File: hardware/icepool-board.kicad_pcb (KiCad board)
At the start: 4 copper layers, 66 x 58 mm, 185 parts, among them J1 USB Micro, J2 PWR_IN, J3 SWD, J4 I2C, J5 RS485, SW1 B3U-1000P, U1 ATSAMD21E, U2 ISL83485, U3 iCE40HX8K-BG121(121-Ball_caBG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, U4 iCE40HX8K-BG121(121-Ball_caBG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, U5 iCE40HX8K-BG121(121-Ball_caBG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, U6 iCE40HX8K-BG121(121-Ball_caBG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, U7 FAN2306, U8 TPS715_SC70, U9 FAN2306, X1 CB3LV-3I-16M0000, X2 CB3LV-3I-16M0000, X3 CB3LV-3I-16M0000, X4 CB3LV-3I-16M0000, Y1 16MHz

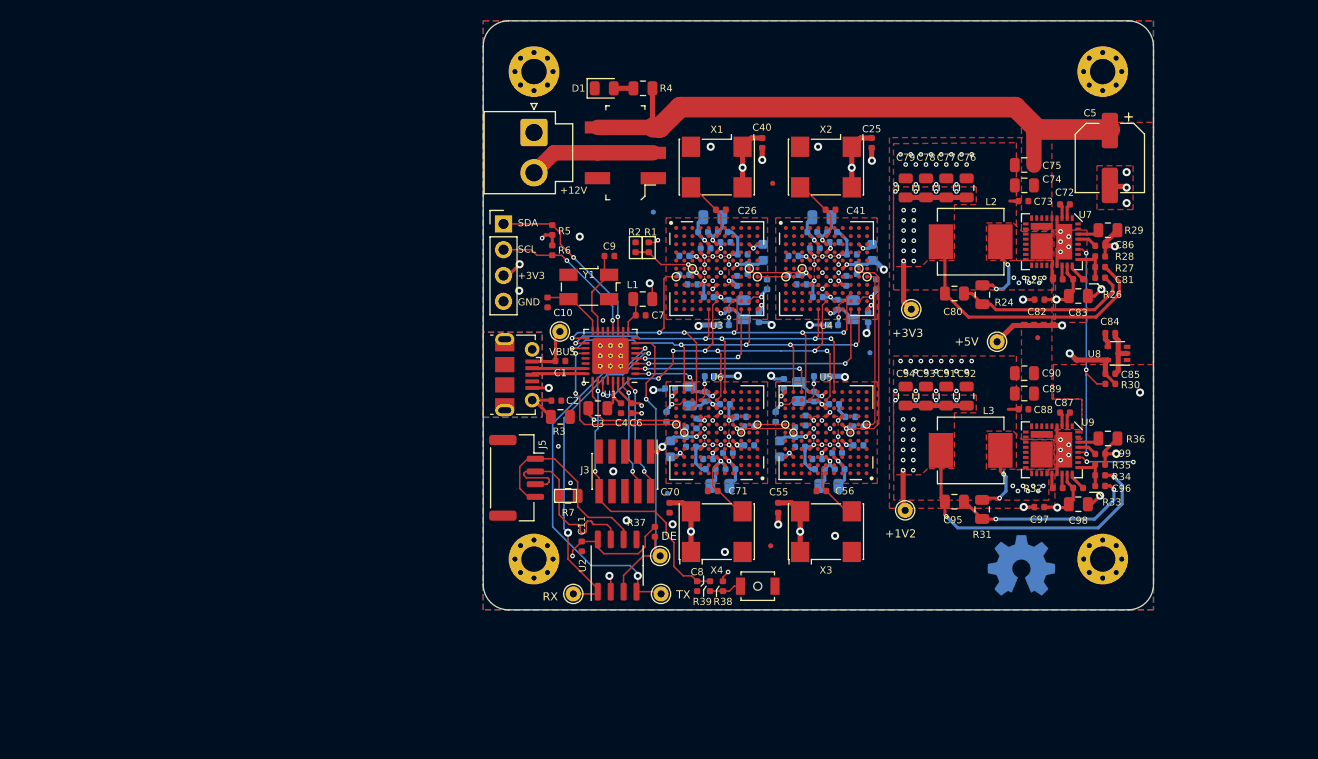
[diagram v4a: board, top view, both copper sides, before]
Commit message: Starting to re-layout. Removed PWR switch.
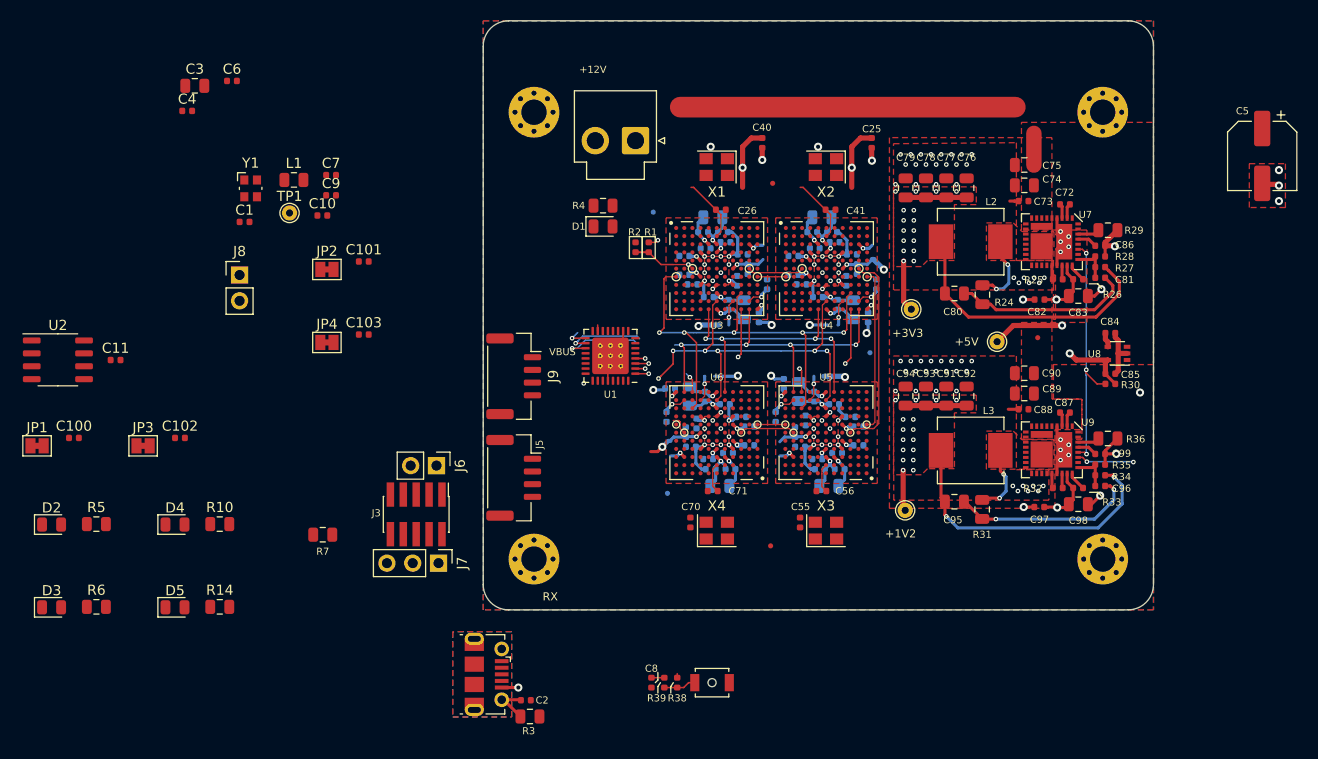
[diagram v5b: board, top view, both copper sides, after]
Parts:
- removed J4: I2C, Connector_PinHeader_2.54mm:PinHeader_1x04_P2.54mm_Vertical
- removed R18, R22, R37: 4k7, Resistor_SMD:R_0402_1005Metric
- removed REF**: OSHW-Symbol_6.7x6mm_Copper, Symbol:OSHW-Symbol_6.7x6mm_Copper
- removed S1: JS202011SCQN, digikey-footprints:Switch_Slide_JS202011SCQN
- removed TP2: RX, TestPoint:TestPoint_THTPad_D1.5mm_Drill0.7mm
- removed TP3: TX, TestPoint:TestPoint_THTPad_D1.5mm_Drill0.7mm
- removed TP7: DE, TestPoint:TestPoint_THTPad_D1.5mm_Drill0.7mm
- added C100: 0.1u, Capacitor_SMD:C_0402_1005Metric, F.Cu at (69.7, 123.1)
- added C101: 0.1u, Capacitor_SMD:C_0402_1005Metric, F.Cu at (98.2, 105.7)
- added C102: 0.1u, Capacitor_SMD:C_0402_1005Metric, F.Cu at (80.1, 123.1)
- added C103: 0.1u, Capacitor_SMD:C_0402_1005Metric, F.Cu at (98.2, 112.9)
- added J6: PWR_ALT, Connector_PinHeader_2.54mm:PinHeader_1x02_P2.54mm_Vertical, F.Cu at (105.4, 125.8)
- added J7: SWD_ALT, Connector_PinHeader_2.54mm:PinHeader_1x03_P2.54mm_Vertical, F.Cu at (105.6, 135.4)
- added J8: UART, Connector_PinHeader_2.54mm:PinHeader_1x02_P2.54mm_Vertical, F.Cu at (86.0, 107.0)
- added J9: RS485_OUT, Connector_JST:JST_GH_SM04B-GHS-TB_1x04-1MP_P1.25mm_Horizontal, F.Cu at (113.0, 117.0)
- added JP1: CUT_2V5, Jumper:SolderJumper-2_P1.3mm_Bridged_Pad1.0x1.5mm, F.Cu at (66.1, 123.8)
- added JP2: CUT_2V5, Jumper:SolderJumper-2_P1.3mm_Bridged_Pad1.0x1.5mm, F.Cu at (94.6, 106.5)
- added JP3: CUT_2V5, Jumper:SolderJumper-2_P1.3mm_Bridged_Pad1.0x1.5mm, F.Cu at (76.5, 123.8)
- added JP4: CUT_2V5, Jumper:SolderJumper-2_P1.3mm_Bridged_Pad1.0x1.5mm, F.Cu at (94.6, 113.7)
- C10, C9: value 15p -> 8p
- C26, C41, C56, C71: value 22p -> DNP
- D2, D3, D4, D5: value CDBU0520 -> LED_IND; footprint Diode_SMD:D_0603_1608Metric -> LED_SMD:LED_0805_2012Metric; moved to F.Cu
- J5: value RS485 -> RS485_IN
- R10, R14: value 4k7 -> 1k; footprint Resistor_SMD:R_0402_1005Metric -> Resistor_SMD:R_0805_2012Metric; moved to F.Cu
- R25, R32: value 1.54k -> 1.50k
- R29: value 56R -> 56k
- R36: value 20R -> 20k
- R5, R6: value 4k7 -> 1k; footprint Resistor_SMD:R_0402_1005Metric -> Resistor_SMD:R_0805_2012Metric
- U2: value ISL83485 -> ISL83488
- X1, X2, X3, X4: value CB3LV-3I-16M0000 -> ASEM1-12.000MHZ; footprint Oscillator:Oscillator_SMD_Abracon_ASV-4Pin_7.0x5.1mm -> Oscillator:Oscillator_SMD_Abracon_ASE-4Pin_3.2x2.5mm
- Y1: footprint Crystal:Crystal_SMD_Abracon_ABM3B-4Pin_5.0x3.2mm -> Crystal:Crystal_SMD_Abracon_ABM10-4Pin_2.5x2.0mm
- moved D3 88.0 mm to (67.5, 139.8), turned to 0 degrees
- moved D2 75.0 mm to (67.5, 131.6), turned to 0 degrees
- moved R14 66.5 mm to (84.1, 139.7)
- moved D4 60.0 mm to (79.7, 131.6), turned to 0 degrees
- moved U2 58.7 mm to (68.1, 115.4), turned to 0 degrees
- moved R6 57.0 mm to (71.9, 139.7), turned to 0 degrees
- moved R5 53.4 mm to (71.9, 131.6), turned to 0 degrees
- moved R10 53.4 mm to (84.1, 131.6)
- moved C4 51.8 mm to (80.8, 90.9), turned to 0 degrees
- moved D5 51.2 mm to (79.7, 139.8), turned to 0 degrees
- moved C6 50.8 mm to (85.3, 87.9), turned to 0 degrees
- moved C3 50.8 mm to (81.6, 88.4)
- moved C11 49.4 mm to (73.8, 115.4), turned to 0 degrees
- moved L1 36.3 mm to (91.4, 97.7)
- moved Y1 34.7 mm to (87.1, 98.5), turned to 0 degrees
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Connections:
- D2 pad 1: /ICE40HX8K-BG121_0/VPP_2V5 -> /ICE40HX8K-BG121_0/LED_IND
- D2 pad 2: +3V3 -> Net-(D2-Pad2)
- D3 pad 1: /ICE40HX8K-BG121_1/VPP_2V5 -> /ICE40HX8K-BG121_1/LED_IND
- D3 pad 2: +3V3 -> Net-(D3-Pad2)
- D4 pad 1: /ICE40HX8K-BG121_2/VPP_2V5 -> /ICE40HX8K-BG121_2/LED_IND
- D4 pad 2: +3V3 -> Net-(D4-Pad2)
- D5 pad 1: /ICE40HX8K-BG121_3/VPP_2V5 -> /ICE40HX8K-BG121_3/LED_IND
- D5 pad 2: +3V3 -> Net-(D5-Pad2)
- J5 pad 1: /DS+ -> /RX+
- J5 pad 2: /DS- -> /RX-
- J5 pad 3: /DS- -> /TX+
- J5 pad 4: /DS+ -> /TX-
- R10 pad 1: +3V3 -> Net-(D4-Pad2)
- R10 pad 2: Net-(R10-Pad2) -> +3V3
- R11 pad 2: /ICE40HX8K-BG121_0/SPI_SS_B -> /SPI_SS_B_0
- R14 pad 1: +3V3 -> Net-(D5-Pad2)
- R14 pad 2: Net-(R14-Pad2) -> +3V3
- R15 pad 2: /ICE40HX8K-BG121_1/SPI_SS_B -> /SPI_SS_B_1
- R19 pad 2: /ICE40HX8K-BG121_2/SPI_SS_B -> /SPI_SS_B_2
- R23 pad 2: /ICE40HX8K-BG121_3/SPI_SS_B -> /SPI_SS_B_3
- R5 pad 1: +3V3 -> Net-(D2-Pad2)
- R5 pad 2: /I2C_SDA -> +3V3
- R6 pad 1: +3V3 -> Net-(D3-Pad2)
- R6 pad 2: /I2C_SCL -> +3V3
- R7 pad 1: /DS+ -> /RX-
- R7 pad 2: /DS- -> /RX+
- U1 pad 1: /CRESET_B_3 -> /SPI_SS_B_3
- U1 pad 13: Net-(U1-Pad13) -> /CDONE
- U1 pad 14: Net-(U1-Pad14) -> /CRESET_B
- U1 pad 2: /CRESET_B_2 -> /SPI_SS_B_2
- U1 pad 3: /CRESET_B_1 -> /SPI_SS_B_1
- U1 pad 4: /CRESET_B_0 -> /SPI_SS_B_0
- U1 pad 5: /RX -> /TX
- U1 pad 6: /TX -> /XCK
- U1 pad 7: /DE -> /RX
- U2 pad 1: /RX -> +3V3
- U2 pad 2: GND -> /RX
- U2 pad 3: /DE -> /TX
- U2 pad 4: /TX -> GND
- U2 pad 5: GND -> /TX-
- U2 pad 6: /DS+ -> /TX+
- U2 pad 7: /DS- -> /RX-
- U2 pad 8: +3V3 -> /RX+
- U3 pad A11: Net-(U3-PadA11) -> /ICE40HX8K-BG121_0/LED_IND
- U3 pad K10: /ICE40HX8K-BG121_0/SPI_SS_B -> /SPI_SS_B_0
- U3 pad K8: Net-(R10-Pad2) -> /CDONE
- U3 pad L9: /CRESET_B_0 -> /CRESET_B
- U4 pad A11: Net-(U4-PadA11) -> /ICE40HX8K-BG121_1/LED_IND
- U4 pad K10: /ICE40HX8K-BG121_1/SPI_SS_B -> /SPI_SS_B_1
- U4 pad K8: Net-(R14-Pad2) -> /CDONE
- U4 pad L9: /CRESET_B_1 -> /CRESET_B
- U5 pad A11: Net-(U5-PadA11) -> /ICE40HX8K-BG121_2/LED_IND
- U5 pad K10: /ICE40HX8K-BG121_2/SPI_SS_B -> /SPI_SS_B_2
- U5 pad K8: Net-(R18-Pad2) -> /CDONE
- U5 pad L9: /CRESET_B_2 -> /CRESET_B
- U6 pad A11: Net-(U6-PadA11) -> /ICE40HX8K-BG121_3/LED_IND
- U6 pad K10: /ICE40HX8K-BG121_3/SPI_SS_B -> /SPI_SS_B_3
- U6 pad K8: Net-(R22-Pad2) -> /CDONE
- U6 pad L9: /CRESET_B_3 -> /CRESET_B
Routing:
- net /TX: track 37.9 -> 0.00 mm, vias 2 -> 0
- net +3V3: track 214.7 -> 179.3 mm, vias 57 -> 49
- net /RX: track 33.3 -> 0.00 mm, vias 2 -> 0
- net /DE: track 31.7 -> 0.00 mm, vias 1 -> 0
- net /~RESET: track 28.3 -> 1.27 mm, vias 2 -> 0
- net /CRESET_B_1: track 26.2 -> 0.00 mm, vias 2 -> 0
- net VCC: track 61.2 -> 37.6 mm
- net /DS-: track 20.4 -> 0.00 mm
- net /DS+: track 19.9 -> 0.00 mm
- net /I2C_SDA: track 18.7 -> 0.00 mm, vias 2 -> 0
- net /CRESET_B_2: track 18.6 -> 0.00 mm, vias 2 -> 0
- net /MISO: track 17.3 -> 0.00 mm, vias 2 -> 0
- net /I2C_SCL: track 15.5 -> 0.00 mm, vias 2 -> 0
- net /CRESET_B: track 0.00 -> 15.4 mm, vias 0 -> 4
- net /CRESET_B_0: track 15.0 -> 0.00 mm, vias 2 -> 0
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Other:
- board text removed: "DE"
- board text removed: "GND"
- board text removed: "SCL"
- board text removed: "SDA"
- board text removed: "TX"

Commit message: Updated layout. Removed fiducials.
Completes issues #19, #20, #21, #22, #23, #24, #26, #27, and #28.
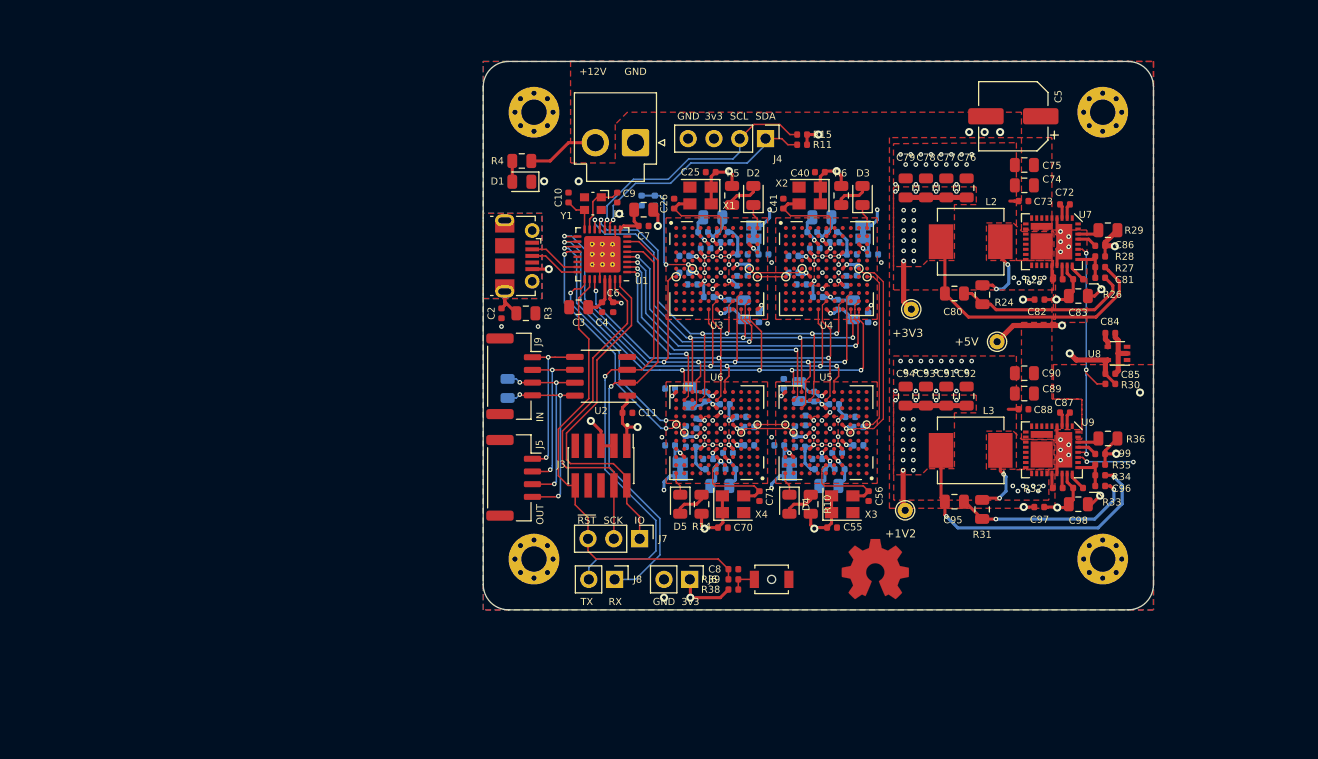
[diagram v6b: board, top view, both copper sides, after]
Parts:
- removed C1: 0.1u, Capacitor_SMD:C_0402_1005Metric
- removed FID1, FID2, FID3, FID4, FID5, FID6: Fiducial, Fiducial:Fiducial_0.5mm_Mask1mm
- removed R19, R23: 4k7, Resistor_SMD:R_0402_1005Metric
- removed TP1: VBUS, TestPoint:TestPoint_THTPad_D1.5mm_Drill0.7mm
- added J4: I2C, Connector_PinHeader_2.54mm:PinHeader_1x04_P2.54mm_Vertical, F.Cu at (137.8, 93.6)
- added REF**: OSHW-Symbol_6.7x6mm_Copper, Symbol:OSHW-Symbol_6.7x6mm_Copper, F.Cu at (148.6, 136.0)
- C10, C9: value 8p -> 18p
- C100, C101, C102, C103, JP1, JP2, JP3, JP4, R1, R2, R7: moved to B.Cu
- R11, R15: moved to F.Cu
- moved D3 89.6 mm to (147.3, 99.2), turned to 90 degrees
- moved R6 83.8 mm to (145.2, 99.2), turned to 90 degrees
- moved D2 76.3 mm to (136.6, 99.2), turned to 90 degrees
- moved JP1 73.7 mm to (136.7, 102.8), turned to 270 degrees
- moved R5 70.5 mm to (134.5, 99.2), turned to 90 degrees
- moved C100 70.3 mm to (137.6, 105.0), turned to 180 degrees
- moved JP3 63.7 mm to (140.2, 126.2), turned to 90 degrees
- moved D4 60.5 mm to (140.2, 129.6), turned to 270 degrees
- moved C102 59.0 mm to (139.2, 123.8)
- moved R10 58.2 mm to (142.2, 129.6), turned to 270 degrees
- moved U2 53.5 mm to (121.6, 117.0), turned to 180 degrees
- moved JP2 52.9 mm to (147.4, 102.8), turned to 270 degrees
- moved D5 50.8 mm to (129.4, 129.6), turned to 270 degrees
- moved C11 50.7 mm to (124.2, 120.6)
- moved C101 50.2 mm to (148.4, 105.0), turned to 180 degrees
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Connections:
- J1 pad 1: /USB_VBUS -> Net-(J1-Pad1)
- J2 pad 2: /VPWR -> VCC
- J5 pad 1: /RX+ -> /TX-
- J5 pad 2: /RX- -> /TX+
- J5 pad 3: /TX+ -> /RX-
- J5 pad 4: /TX- -> /RX+
- J9 pad 1: /RX+ -> /TX-
- J9 pad 2: /RX- -> /TX+
- J9 pad 3: /TX+ -> /RX-
- J9 pad 4: /TX- -> /RX+
- R11 pad 1: GND -> +3V3
- R11 pad 2: /SPI_SS_B_0 -> /I2C_SDA
- R15 pad 1: GND -> +3V3
- R15 pad 2: /SPI_SS_B_1 -> /I2C_SCL
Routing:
- net /TX: track 0.00 -> 45.8 mm, vias 0 -> 1
- net /~RESET: track 1.27 -> 46.1 mm
- net /RX: track 0.00 -> 43.6 mm, vias 0 -> 1
- net /CDONE: track 10.1 -> 52.5 mm, vias 4 -> 5
- net /CRESET_B: track 15.4 -> 51.2 mm, vias 4 -> 5
- net /SWD_IO: track 0.00 -> 34.1 mm
- net /SWD_CLK: track 0.00 -> 33.3 mm
- net /SPI_SS_B_1: track 3.64 -> 33.2 mm
- net VCC: track 37.6 -> 8.52 mm
- net /I2C_SCL: track 0.00 -> 25.7 mm, vias 0 -> 1
- net /SPI_SS_B_2: track 3.31 -> 27.8 mm
- net /MISO: track 0.00 -> 24.1 mm, vias 0 -> 2
- net /I2C_SDA: track 0.00 -> 23.9 mm, vias 0 -> 1
- net /READY: track 1.98 -> 21.7 mm, vias 0 -> 2
- net /RX+: track 0.00 -> 19.4 mm, vias 0 -> 3
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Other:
- board size 66 x 58 mm -> 66 x 54 mm
- board text added: "3v3"
- board text added: "GND"
- board text added: "HI"
- board text added: "IN"
- board text added: "IO"
- board text added: "LO"
- board text added: "OUT"
- board text added: "READY"
- board text added: "RS485 Term."
- board text added: "SCK"
- board text added: "SCL"
- board text added: "SDA"
- board text added: "TX"
- board text added: "icepool 2020-02 fourside.io"
- board text added: "~RST"
- board text removed: "VBUS"
- board text removed: "icepool-board 2020-02 fourside.io"

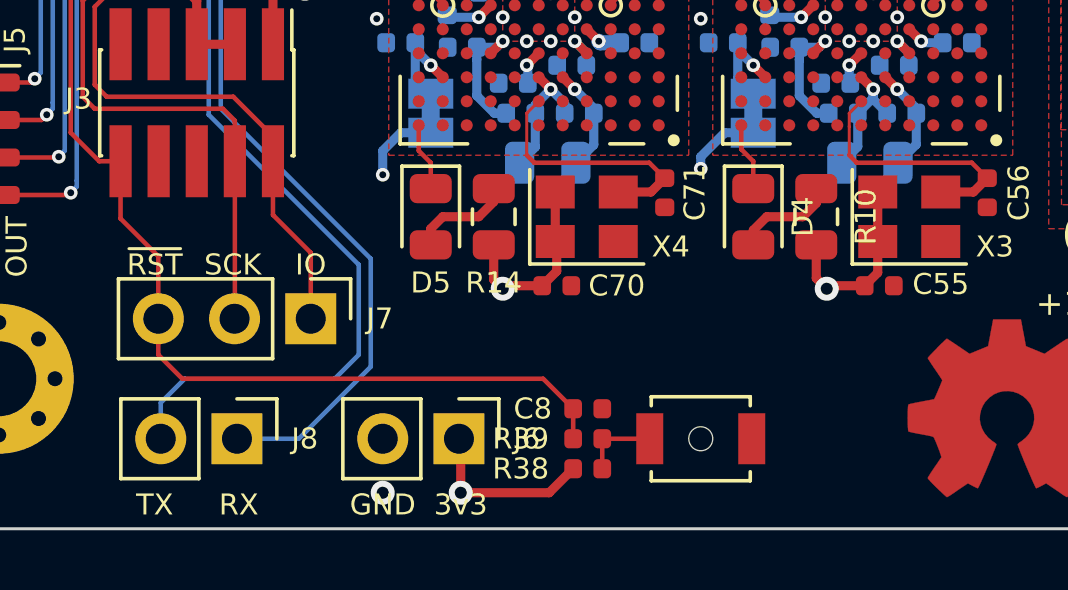
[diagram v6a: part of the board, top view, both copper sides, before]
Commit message: Fixed some label placements.
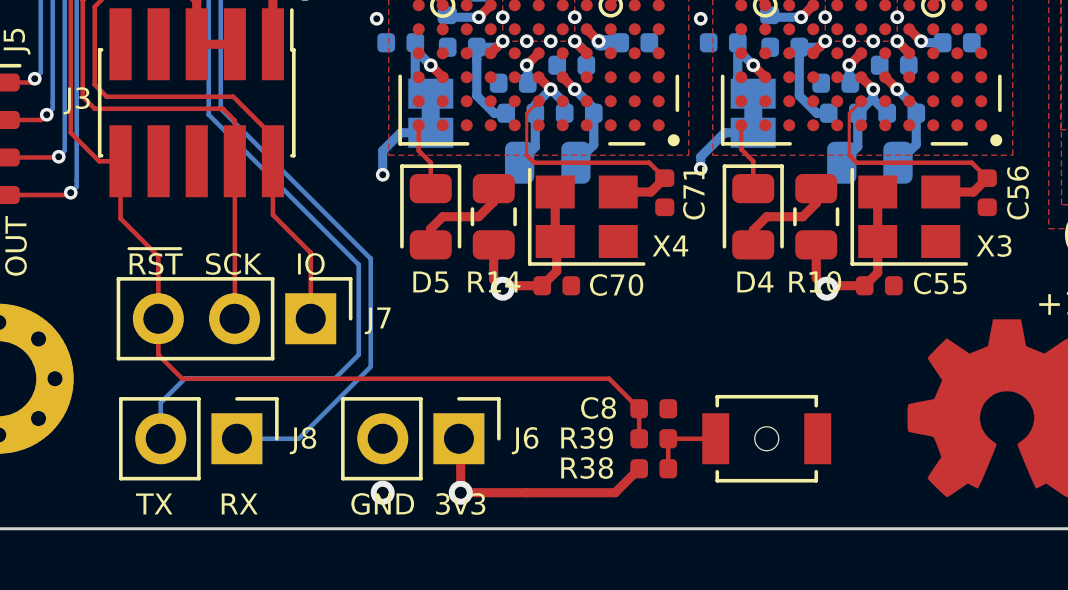
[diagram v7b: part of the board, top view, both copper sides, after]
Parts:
- moved C8 2.20 mm to (136.8, 136.0)
- moved R38 2.20 mm to (136.8, 138.0)
- moved R39 2.20 mm to (136.8, 137.0)
- moved SW1 2.20 mm to (140.6, 137.0)
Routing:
- net /~RESET: track 46.1 -> 48.3 mm
- net +3V3: track 194.6 -> 196.8 mm
